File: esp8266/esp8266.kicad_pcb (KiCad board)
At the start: 4 copper layers, 29 x 49 mm, 38 parts, among them J1 power, J2 TTL, J3 Conn_01x15_Female, J4 Conn_01x15_Female, SW1 RST, SW2 Flash, U1 ESP8266EX, U2 Flash_SOP-8_150mil, Y1 26MHz

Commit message: feat: update esp8266ex
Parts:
- moved D1 59.7 mm to (126.0, 136.8)
- moved R2 59.7 mm to (126.0, 135.8)
- moved R8 59.7 mm to (126.0, 137.8)
- moved R12 42.1 mm to (123.9, 117.6)
- moved R1 41.8 mm to (123.9, 119.6)
- moved R4 41.8 mm to (123.9, 118.6)
- moved SW1 11.4 mm to (124.3, 144.1)
- moved R14 11.2 mm to (129.4, 130.2), turned to 180 degrees
- moved SW2 11.2 mm to (134.6, 144.1)
- moved R15 8.93 mm to (123.9, 116.1), turned to 0 degrees
- moved J4 8.08 mm to (139.5, 115.4)
- moved J3 8.00 mm to (119.2, 115.4)
- moved J1 7.74 mm to (135.5, 150.9)
- moved C8 7.60 mm to (134.1, 121.9), turned to 0 degrees
- moved J2 7.50 mm to (122.8, 151.2)
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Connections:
- R9 pad 1: /nRST -> /RST
- U2 pad 1: Net-(R13-Pad1) -> /MTDO
- U2 pad 2: /MTCK -> /MTDI
- U2 pad 3: /MTDI -> Net-(R14-Pad1)
- U2 pad 5: Net-(R14-Pad1) -> /MTCK
- U2 pad 6: /MTDO -> Net-(R15-Pad1)
- U2 pad 7: Net-(R15-Pad1) -> Net-(R13-Pad1)

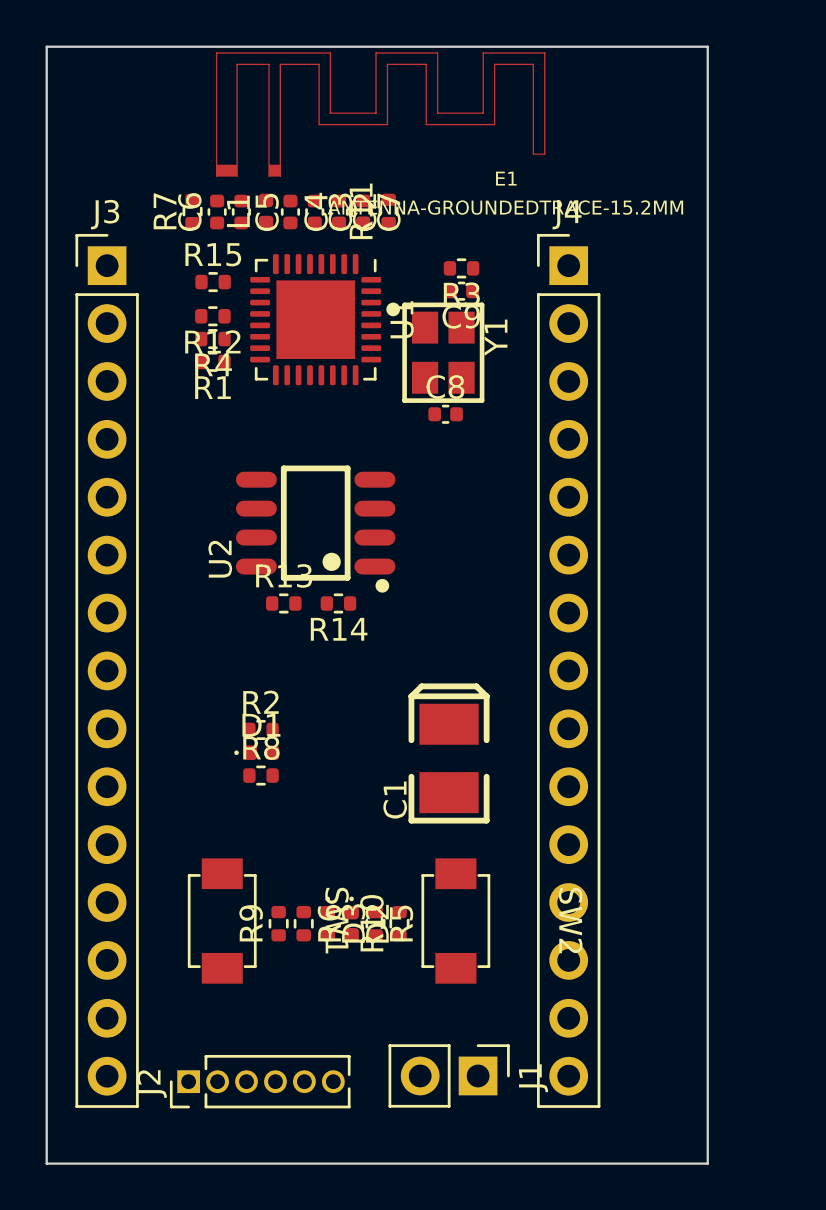
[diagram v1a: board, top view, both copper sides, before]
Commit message: feat 1. add 2.4G wifi  2. update esp8266 board
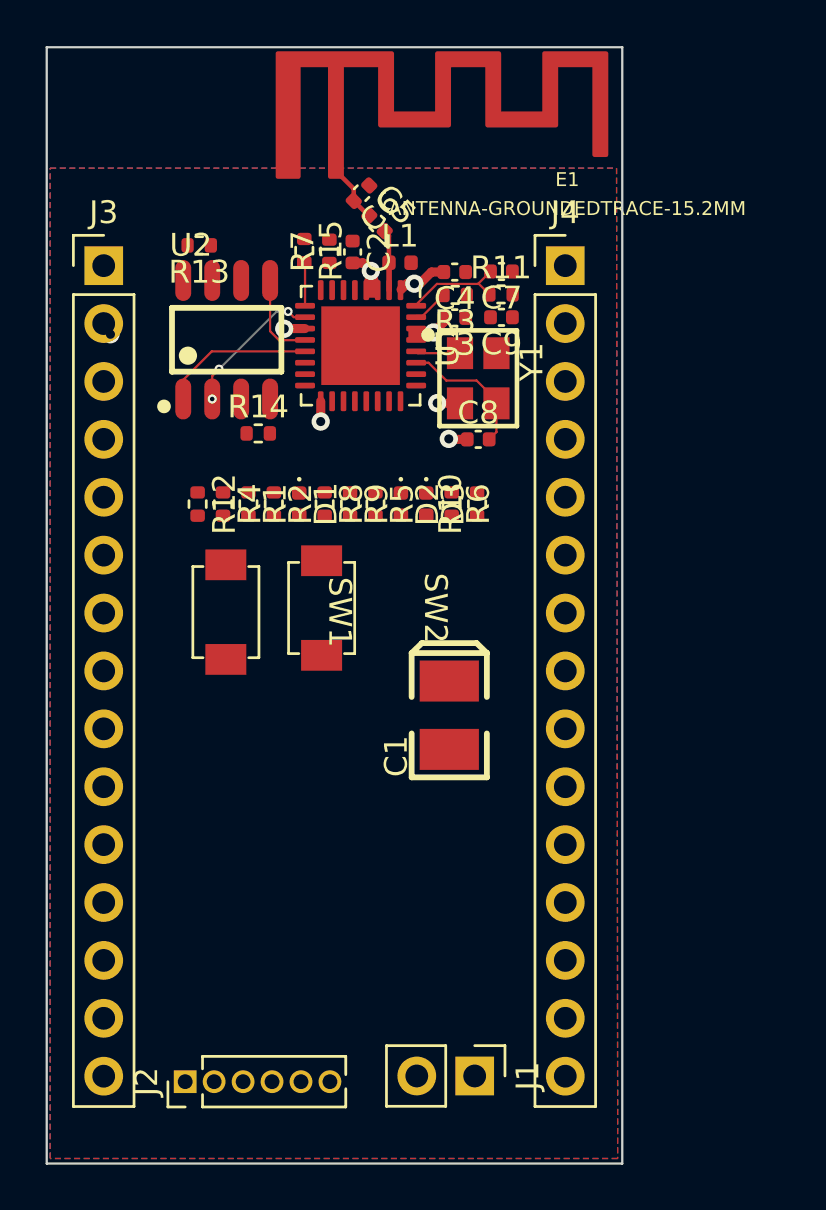
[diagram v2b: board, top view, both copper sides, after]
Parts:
- E1: footprint RF1:TRACE_ANTENNA_2.4GHZ_15.2MM -> My-lib-footprints:RF_2.4GHZ_15.2MM
- moved R6 19.5 mm to (134.4, 125.8)
- moved D3 18.9 mm to (133.3, 125.8)
- moved R10 18.7 mm to (135.5, 125.8)
- moved R9 18.7 mm to (129.9, 125.8), turned to -90 degrees
- moved D2 18.5 mm to (132.1, 125.8)
- moved R5 18.4 mm to (131.0, 125.8)
- moved R13 16.1 mm to (123.3, 114.5), turned to 180 degrees
- moved SW2 14.9 mm to (128.7, 130.4)
- moved SW1 13.6 mm to (124.5, 130.6)
- moved R8 12.2 mm to (128.8, 125.8), turned to -90 degrees
- moved D1 11.0 mm to (127.7, 125.8), turned to -90 degrees
- moved R2 9.93 mm to (126.6, 125.8), turned to -90 degrees
- moved U2 8.94 mm to (124.5, 118.6), turned to 0 degrees
- moved R12 8.27 mm to (123.2, 125.8), turned to -90 degrees
- moved R14 8.25 mm to (125.9, 122.7), turned to 0 degrees
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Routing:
- net +3V3: track 0.00 -> 27.7 mm, vias 0 -> 5
- net /MTDO: track 0.00 -> 6.70 mm
- net /MTDI: track 0.00 -> 6.36 mm, vias 0 -> 3
- net Net-(C8-Pad2): track 0.00 -> 6.05 mm
- net /RST: track 0.00 -> 4.60 mm
- net /MTCK: track 0.00 -> 3.93 mm
- net Net-(C5-Pad2): track 0.00 -> 2.65 mm
- net Net-(C5-Pad1): track 0.00 -> 2.60 mm
- net Net-(R3-Pad2): track 0.00 -> 2.00 mm
- net Net-(C9-Pad2): track 0.00 -> 1.96 mm
- net /MTMS: track 0.00 -> 1.92 mm
- net GND: track 0.00 -> 1.82 mm, vias 0 -> 2
- net unconnected-(J3-Pad2): track 0.00 -> 0.01 mm, vias 0 -> 1
- added copper zone on In2.Cu, net +3V3
- added copper zone on B.Cu, net GND
- added copper zone on F.Cu, net GND
- added copper zone on In1.Cu, net GND
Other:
- board size 29 x 49 mm -> 25.2 x 49 mm

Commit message: feat: update esp 8266
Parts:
- moved SW2 7.03 mm to (134.6, 134.2)
- moved C1 4.76 mm to (129.5, 134.9)
- moved SW1 3.66 mm to (124.5, 134.2)
- moved R14 1.58 mm to (124.3, 122.8), turned to 180 degrees
- moved D2 0.16 mm to (132.0, 125.8)
- moved R5 0.14 mm to (130.9, 125.8)
- moved R9 0.12 mm to (129.8, 125.8)
- moved R8 0.10 mm to (128.7, 125.8)
- moved C2 0.10 mm to (130.0, 114.7)
- moved R13 0.09 mm to (123.3, 114.4)
- moved D1 0.08 mm to (127.6, 125.8)
- moved R7 0.06 mm to (129.0, 114.7)
- moved R2 0.06 mm to (126.5, 125.8)
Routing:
- net +3V3: track 27.7 -> 35.9 mm, vias 5 -> 11
- net /GPIO2: track 0.00 -> 7.29 mm
- net /GPIO0: track 0.00 -> 6.33 mm
- net /MTDO: track 6.70 -> 11.1 mm
- net Net-(R15-Pad1): track 0.00 -> 4.04 mm
- net Net-(C9-Pad2): track 1.96 -> 4.09 mm
- net GND: track 1.82 -> 3.87 mm
- net Net-(R13-Pad1): track 0.00 -> 1.65 mm
- net Net-(R14-Pad1): track 0.00 -> 1.65 mm
- net /CHIP_PU: track 0.00 -> 1.31 mm
- net /GPIO16: track 0.00 -> 1.10 mm
- net /MTMS: track 1.92 -> 2.54 mm, vias 0 -> 2
- net /RST: track 4.60 -> 4.64 mm, vias 0 -> 2
- net /MTDI: vias 3 -> 2

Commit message: feat: esp8266 gerber
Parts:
- moved J3 20.6 mm to (139.7, 115.4)
- moved J4 20.5 mm to (118.9, 115.4)
- moved SW1 10.3 mm to (134.6, 132.3)
- moved SW2 9.71 mm to (125.0, 132.3)
- moved R10 9.10 mm to (126.4, 125.9), turned to -90 degrees
- moved J2 6.36 mm to (129.0, 151.2), turned to -90 degrees
- moved R9 5.43 mm to (135.2, 125.9)
- moved R6 3.46 mm to (130.9, 125.9)
- moved R5 3.22 mm to (134.1, 125.9)
- moved C1 1.93 mm to (129.8, 133.0)
- moved D3 1.34 mm to (132.0, 125.9)
- moved R8 1.16 mm to (129.8, 125.9)
- moved D1 1.10 mm to (128.7, 125.9)
- moved D2 1.05 mm to (133.0, 125.9)
- moved R2 1.03 mm to (127.5, 125.9)
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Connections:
- J3 pad 12: /CHIP_PU -> unconnected-(J3-Pad12)
- J4 pad 12: /RXD0 -> /RXD
- J4 pad 13: /TXD0 -> /TXD
- J4 pad 2: /GPIO5 -> unconnected-(J4-Pad2)
- U1 pad 25: /RXD0 -> /RXD
- U1 pad 26: /TXD0 -> /TXD
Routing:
- net /RST: track 4.64 -> 57.7 mm, vias 2 -> 3
- net /RXD: track 0.00 -> 43.4 mm, vias 0 -> 1
- net /TXD: track 0.00 -> 43.4 mm, vias 0 -> 1
- net /GPIO0: track 6.33 -> 41.7 mm, vias 0 -> 1
- net /MTCK: track 3.93 -> 30.1 mm
- net /MTMS: track 2.54 -> 25.9 mm
- net /MTDO: track 11.1 -> 32.1 mm
- net /MTDI: track 6.36 -> 26.6 mm, vias 2 -> 3
- net /GPIO16: track 1.10 -> 20.6 mm, vias 0 -> 2
- net /SCLK: track 0.00 -> 18.1 mm, vias 0 -> 1
- net /SD0/MISO: track 0.00 -> 15.4 mm, vias 0 -> 1
- net /CMD/MOSI: track 0.00 -> 15.0 mm, vias 0 -> 2
- net /SD2/GPIO9: track 0.00 -> 13.4 mm, vias 0 -> 1
- net /ADC_IN: track 0.00 -> 12.8 mm, vias 0 -> 2
- net /SD1/INT: track 0.00 -> 12.0 mm, vias 0 -> 1
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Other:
- board text added: "+"
- board text added: "-"
- board text added: "3.3"
- board text added: "CMD"
- board text added: "DCIN"
- board text added: "GND"
- board text added: "GPIO0"
- board text added: "IO0"
- board text added: "IO16"
- board text added: "IO2"
- board text added: "IO4"
- board text added: "IO9"
- board text added: "MTCK"
- board text added: "MTDI"
- board text added: "MTDO"
- board text added: "MTMS"
- board text added: "RST"
- board text added: "RXD"
- board text added: "Rev"
- board text added: "SCLK"
- board text added: "SD0"
- board text added: "SD1"
- board text added: "SD3"
- board text added: "TXD"
